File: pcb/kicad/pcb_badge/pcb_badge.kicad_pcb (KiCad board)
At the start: 2 copper layers, 82 x 132 mm, 254 parts, among them J1 DEALON USB-TYPE-C-018, J2 Conn_01x02_Pin, J3 Conn_01x04_Pin, J4 Conn_01x03_Pin, J5 Conn_01x03_Pin, J7 Conn_01x02_Pin, Q1 SI2302, Q2 JSM2301S, Q9 2N7002, Q90 2N7002, Q91 2N7002, Q910 2N7002, Q911 2N7002, Q912 2N7002, Q913 2N7002, Q914 2N7002, Q915 2N7002, Q92 2N7002, Q93 2N7002, Q94 2N7002, Q95 2N7002, Q96 2N7002, Q97 2N7002, Q98 2N7002, Q99 2N7002, SW1 SW_MEC_5E, SW2 SW_MEC_5E, SW3 SW_MEC_5E, SW4 SW_MEC_5E, SW5 SW_MEC_5E, SW6 SW_MEC_5E, SW7 SW_MEC_5E, SW8 SW_MEC_5E, U1 TLV70328DBVR, U2 QX2304L33F, U3 STM32F103CBT6, U4 74HC238, U5 LSM6DS3TR-C, U6 IRM-H638T/TR2, U8 74HC238, Y1 TAXM8M4RFDCET2T

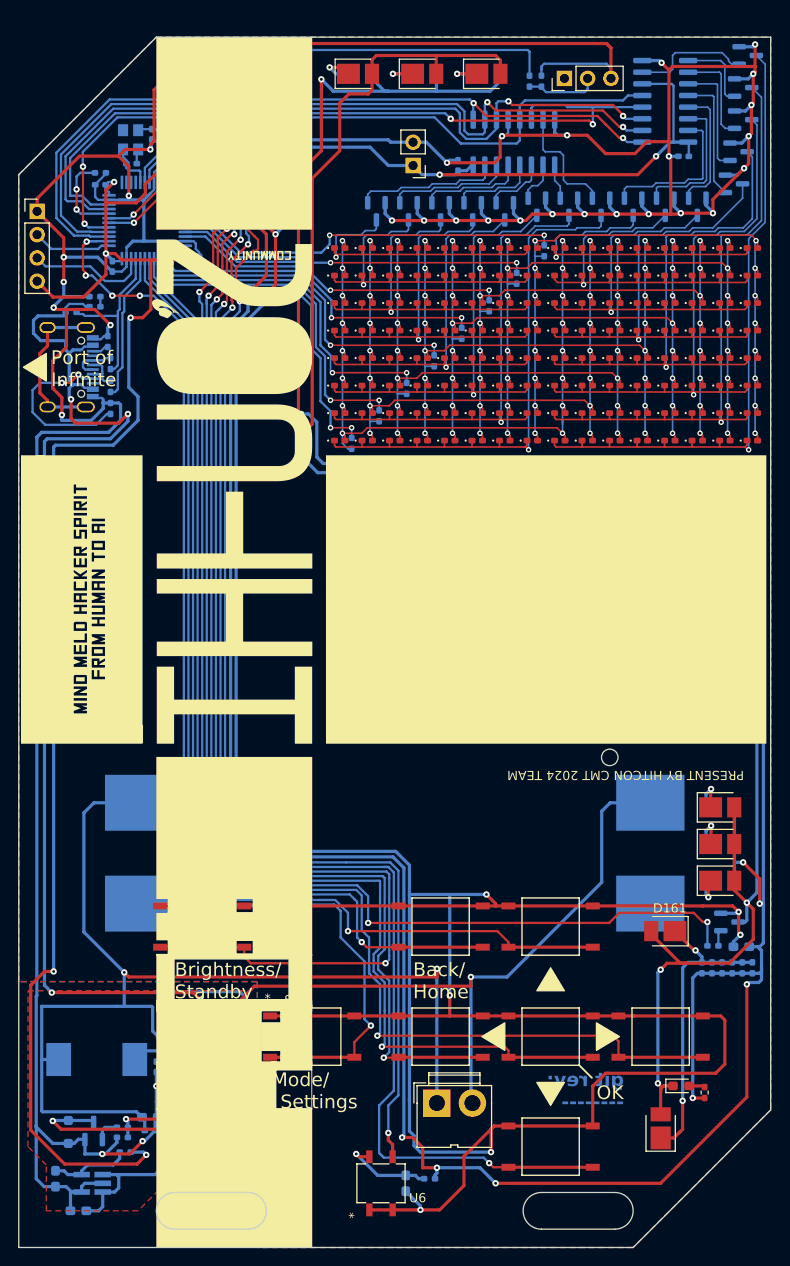
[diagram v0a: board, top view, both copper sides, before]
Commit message: Implement new board graphics design
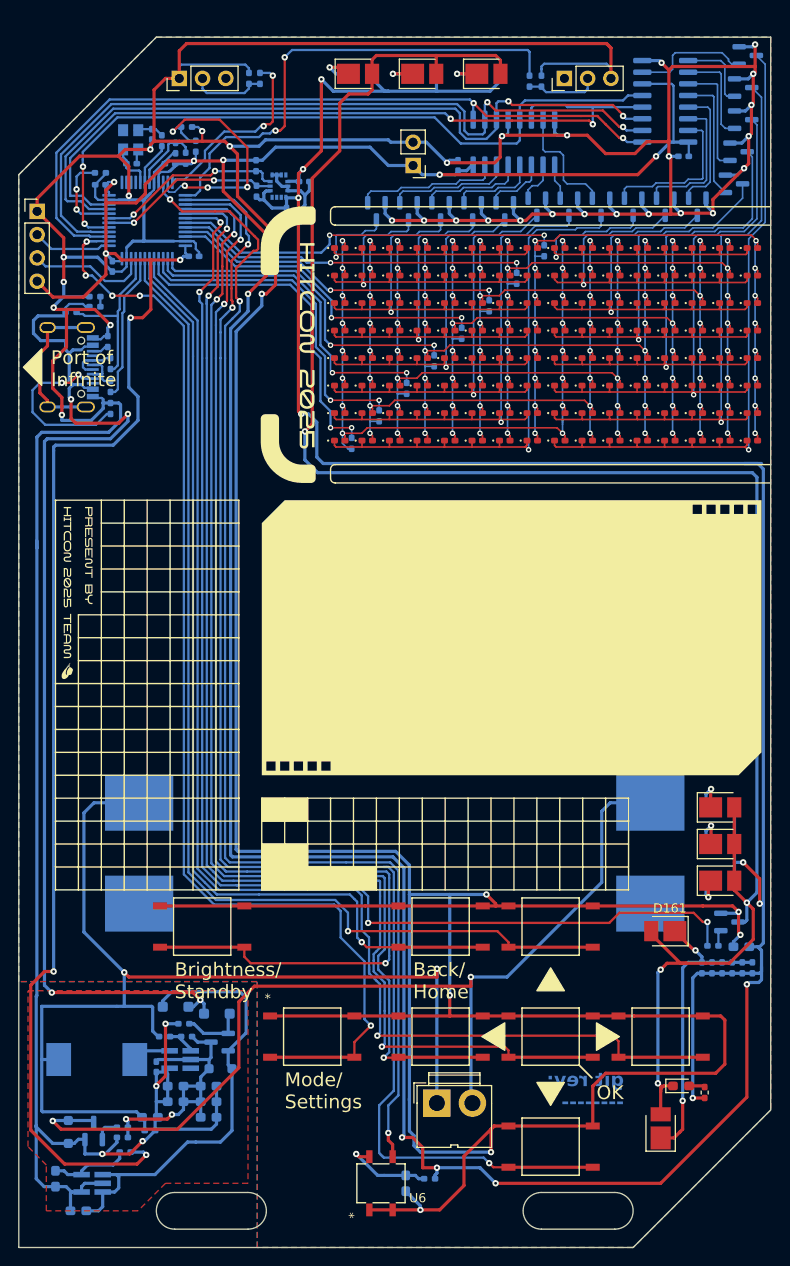
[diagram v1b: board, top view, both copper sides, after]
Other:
- board text added: "Mode/ Settings"
- board text removed: "Mod Set"
- board text removed: "PRESENT BY HITCON CMT 2024 TEAM"
- board text removed: "e/ tings"

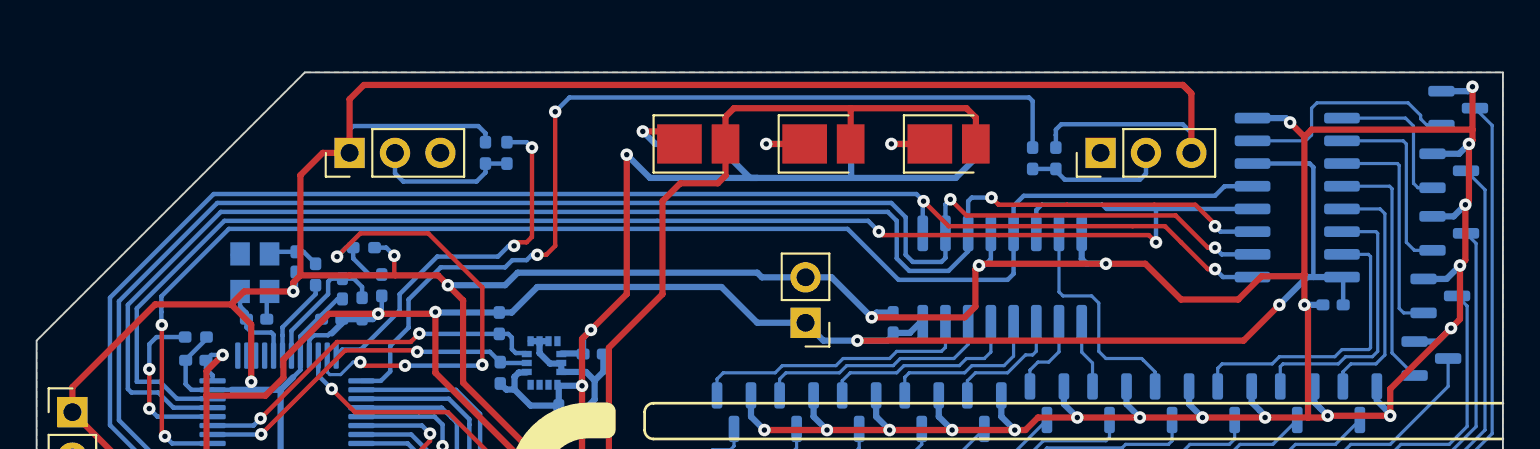
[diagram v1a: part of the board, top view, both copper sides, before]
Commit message: Expand PCB Size
Expand PCB Size to compensate cross-board header position
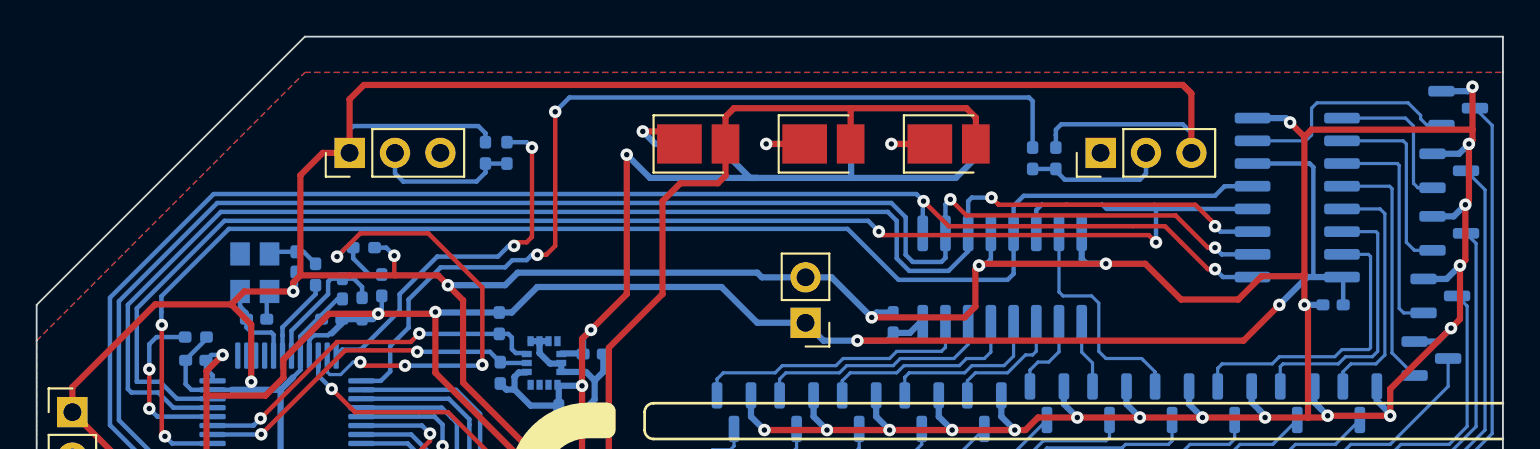
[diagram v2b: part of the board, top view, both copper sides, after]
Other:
- board size 82 x 132 mm -> 82 x 134 mm
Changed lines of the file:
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@@
 		(layer "Dwgs.User")
+	)
+	(gr_line
+		(start 74 43)
+		(end 74.000002 45)
+		(stroke
+			(width 0.1)
+			(type default)
+		)
+		(layer "Edge.Cuts")
 	)
 	(gr_arc
@@
 	)
 	(gr_line
-		(start 89.000002 30)
-		(end 156.000002 30)
-		(stroke
-			(width 0.1)
-			(type default)
-		)
-		(layer "Edge.Cuts")
-	)
-	(gr_line
 		(start 74.000002 45)
 		(end 74.000002 162)
@@
 		(start 131 156)
 		(end 139 156)
+		(stroke
+			(width 0.1)
+			(type default)
+		)
+		(layer "Edge.Cuts")
+	)
+	(gr_line
+		(start 156 28)
+		(end 89 28)
 		(stroke
 			(width 0.1)
@@
 	)
 	(gr_line
+		(start 156.000002 30)
+		(end 156 28)
+		(stroke
+			(width 0.1)
+			(type default)
+		)
+		(layer "Edge.Cuts")
+	)
+	(gr_line
 		(start 74.000002 162)
 		(end 141.000002 162)
@@
 	)
 	(gr_line
-		(start 89.000002 30)
-		(end 74.000002 45)
+		(start 89 28)
+		(end 74 43)
 		(stroke
 			(width 0.1)

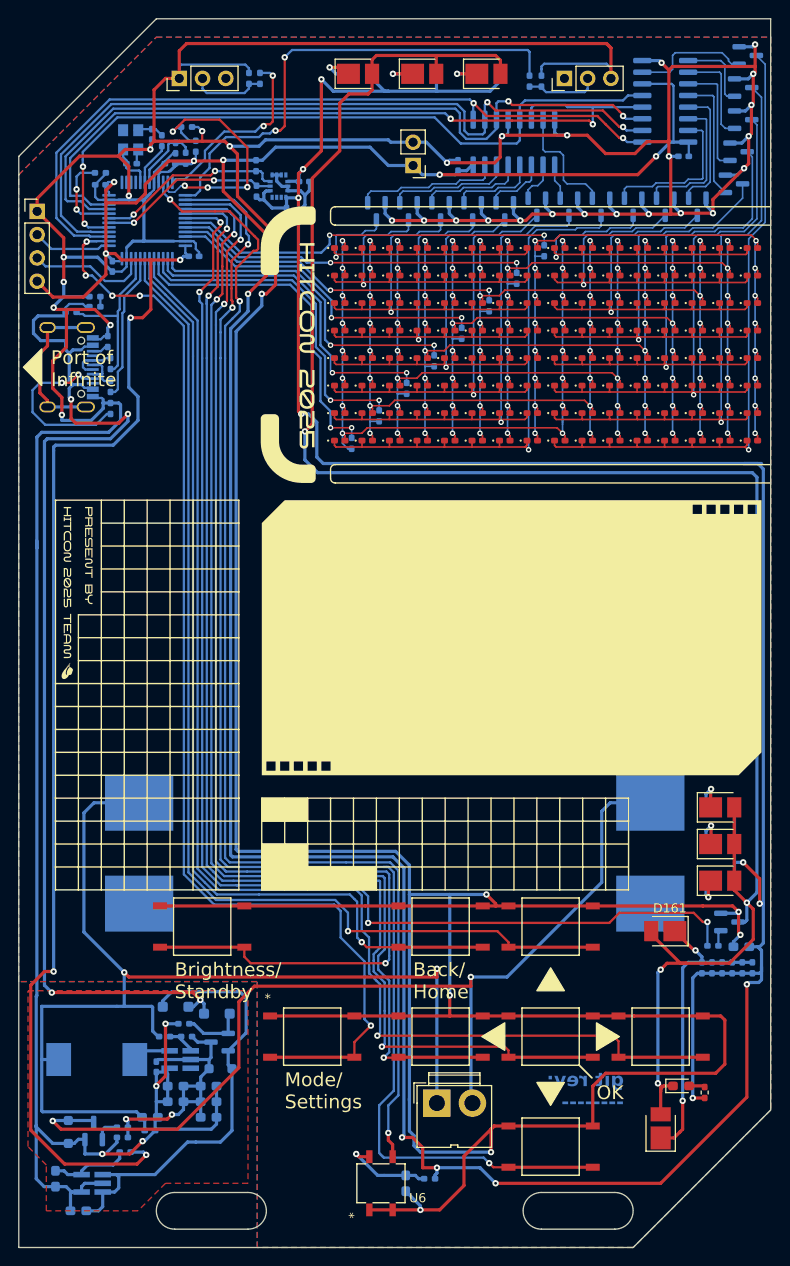
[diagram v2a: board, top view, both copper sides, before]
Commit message: pcb: Zone fill and pass DRC check
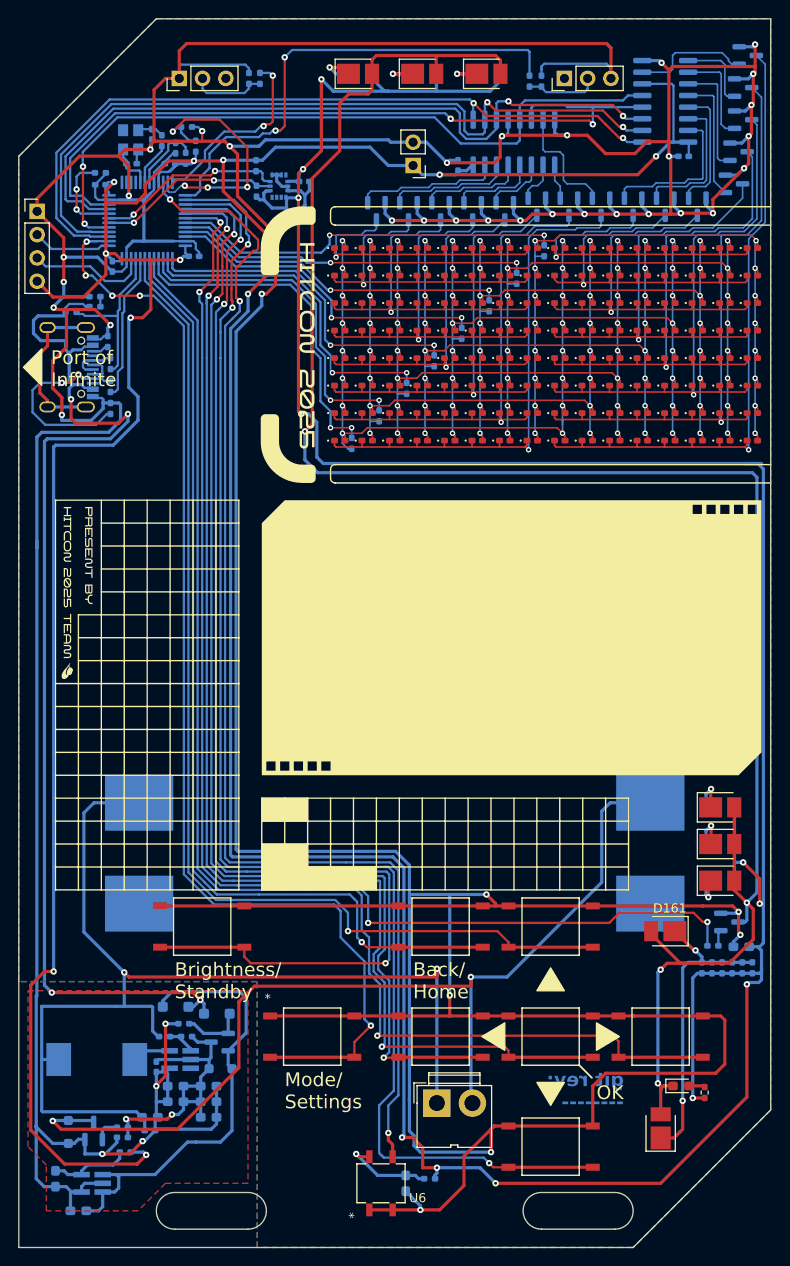
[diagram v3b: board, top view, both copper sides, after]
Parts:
- moved C51 0.76 mm to (103.9, 49.0), turned to 0 degrees
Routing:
- net GND: track 898.6 -> 894.8 mm

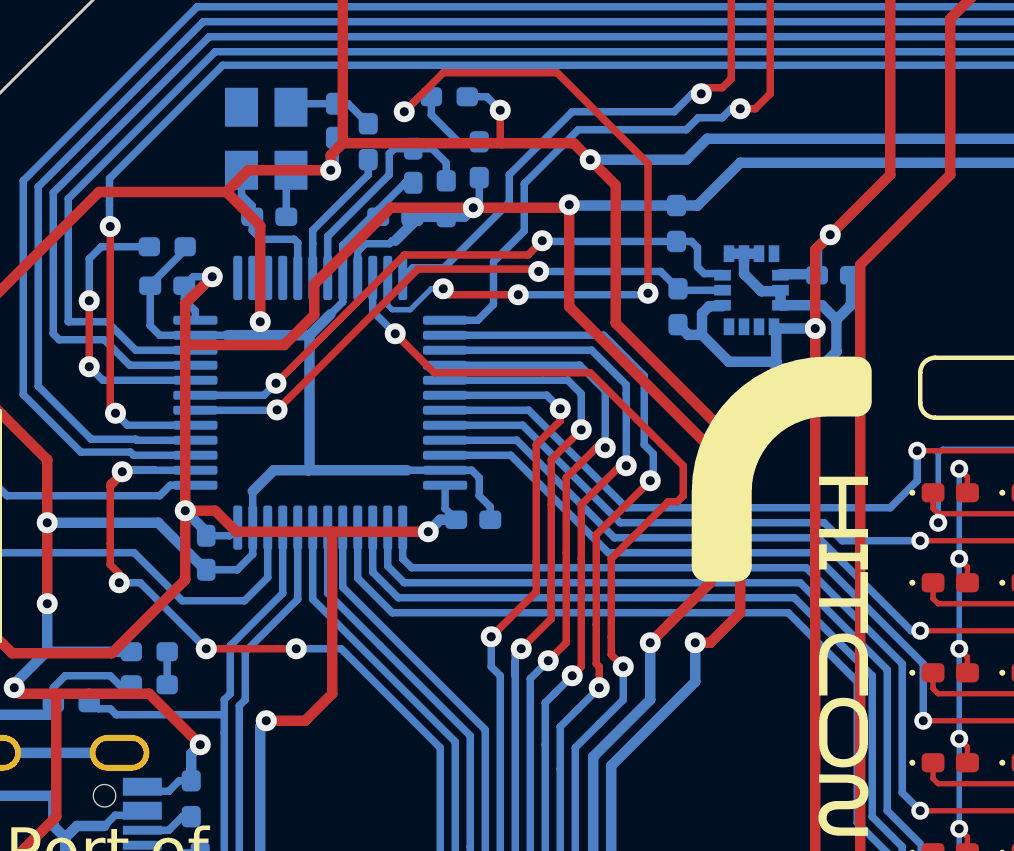
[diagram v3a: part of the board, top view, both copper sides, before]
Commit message: pcb: Connect accelerometer INT1
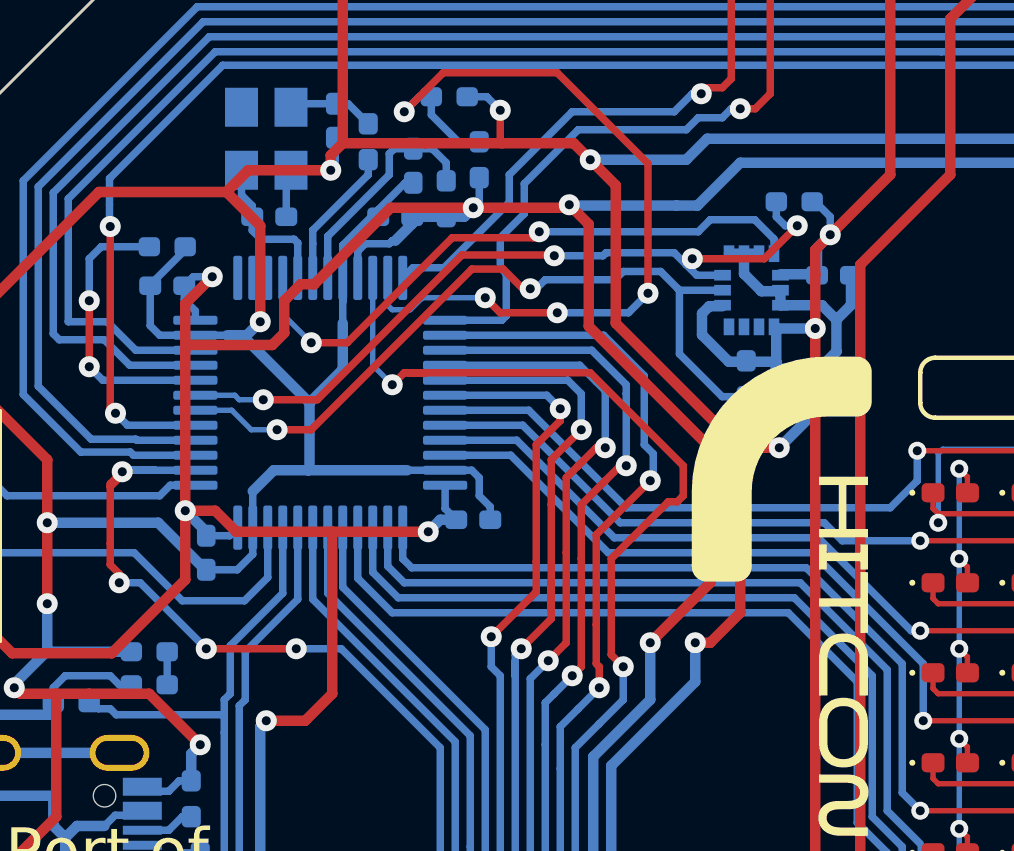
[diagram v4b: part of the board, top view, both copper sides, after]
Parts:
- moved R50 3.99 mm to (103.8, 43.3), turned to 0 degrees
- moved R51 3.31 mm to (102.2, 49.2), turned to 90 degrees
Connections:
- U3 pad 4: unconnected-(U3-PC15-Pad4) -> /MCU/ACC_INT1
- U5 pad 4: unconnected-(U5-INT1-Pad4) -> /MCU/ACC_INT1
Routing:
- net /MCU/ACC_INT1: track 0.00 -> 20.4 mm, vias 0 -> 2
- net GND: track 894.8 -> 901.2 mm
- net /MCU/I2C1_SCL: track 19.9 -> 25.8 mm
- net /MCU/I2C1_SDA: track 20.6 -> 25.6 mm, vias 2 -> 4
- net /MCU/IRRX: track 134.3 -> 136.3 mm
- net /MCU/PA3: track 52.9 -> 53.6 mm

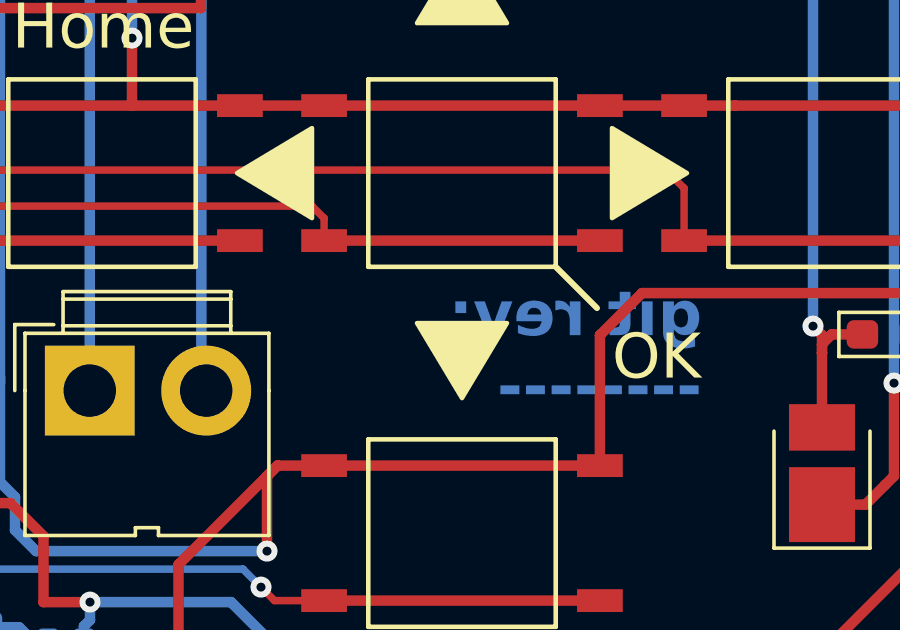
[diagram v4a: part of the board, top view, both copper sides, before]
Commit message: pcb: Added markings on version
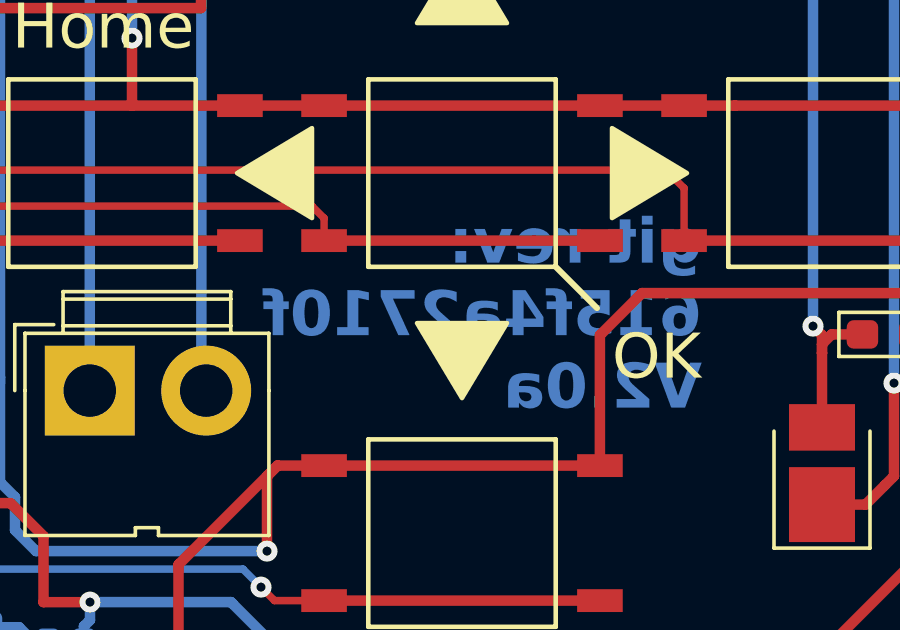
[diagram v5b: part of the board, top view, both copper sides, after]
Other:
- board text added: "git rev: 615f4a"
- board text added: "git rev: 615f4a2710f V2.0a"
- board text removed: "git rev: --------"
